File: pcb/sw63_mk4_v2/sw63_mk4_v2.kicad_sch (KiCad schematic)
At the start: 70 parts, among them J1 GT-USB-7070C, J2 SWD, J3 Conn_01x02, Q1 DMG2305UX-7, Q2 DMG2302U-7, Q3 TEMT6200FX01, SW1 KSC321J LFS, SW2 ﻿EVQ-P7J01P, U1 DIO5518BST5, U2 MCP1711T-3.3I/OT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

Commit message: schematic notes
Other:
- note added: "Compatible LED drivers: TLC5916IPWR TLC5917IPWR SCT2167CSSG STP08CP05TTR"
- note added: "R3: 22k = approx 50mA charge current"
- note removed: "22k = approx 50mA charge current"
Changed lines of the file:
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@@
 	(text "BAT current when MCU sleeps (BAT is 4V)\nMCP73832T-2ACI/OT: approx 21uA - little worse\nDIO5518BST5: approx 15uA (10-20 based on ambient temperature) - little better"
 		(exclude_from_sim no)
-		(at 235.712 24.638 0)
+		(at 192.024 26.162 0)
 		(effects
 			(font
@@
 				(thickness 0.1588)
 			)
+			(justify left)
 		)
 	)
@@
 		)
 	)
-	(text "22k = approx 50mA charge current"
+	(text "R3: 22k = approx 50mA charge current"
 		(exclude_from_sim no)
-		(at 237.236 29.464 0)
+		(at 169.164 67.564 0)
 		(effects
 			(font
@@
 				(thickness 0.1588)
 			)
+			(justify left)
 		)
 	)
+	(text "Compatible LED drivers:\nTLC5916IPWR\nTLC5917IPWR\nSCT2167CSSG\nSTP08CP05TTR"
+		(exclude_from_sim no)
+		(at 211.074 133.858 0)
+		(effects
+			(font
+				(size 1.27 1.27)
+				(thickness 0.1588)
+			)
+			(justify left)
+		)
+	)

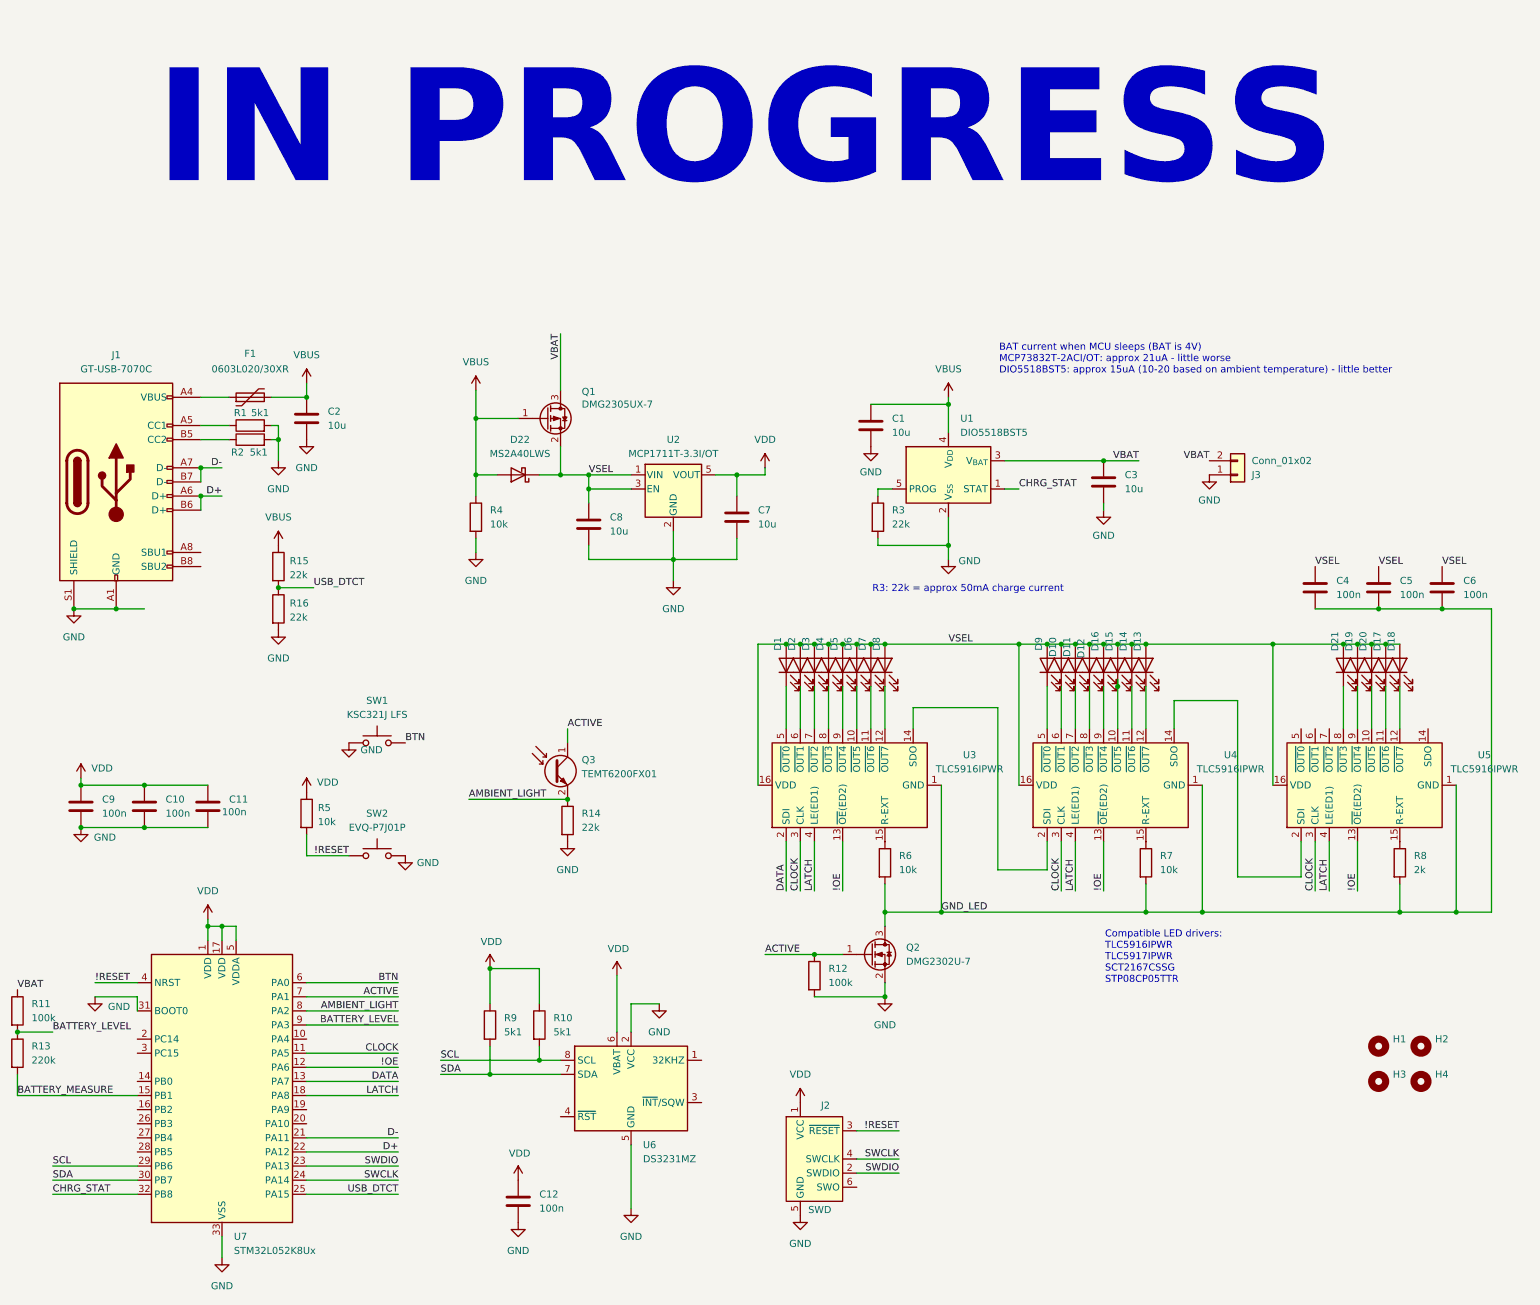
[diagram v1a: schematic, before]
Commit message: update part names and docs
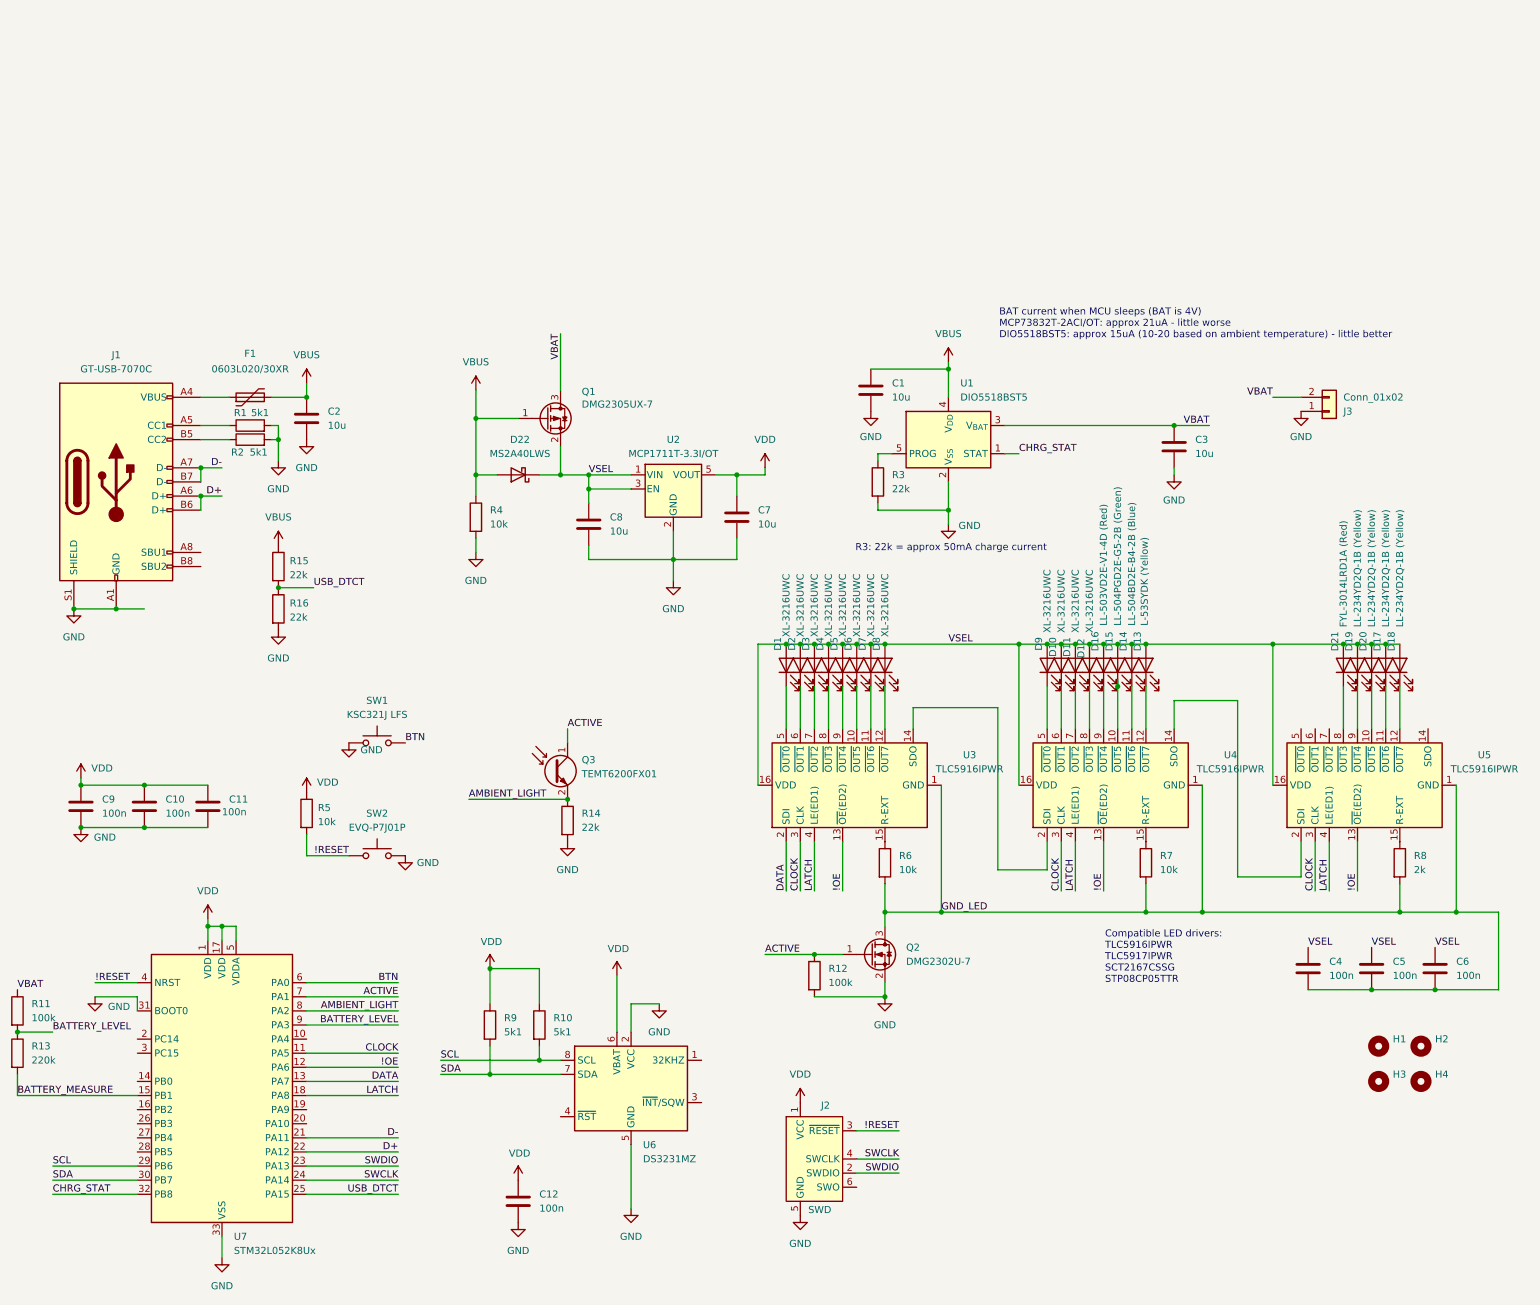
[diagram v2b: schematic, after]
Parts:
- D1, D10, D11, D12, D2, D3, D4, D5, D6, D7, D8, D9: value LED -> XL-3216UWC
- D13: value LED -> L-53SYDK (Yellow)
- D14: value LED -> LL-504BD2E-B4-2B (Blue)
- D15: value LED -> LL-504PGD2E-G5-2B (Green)
- D16: value LED -> LL-503VD2E-V1-4D (Red)
- D17, D18, D19, D20: value LED -> LL-234YD2Q-1B (Yellow)
- D21: value LED -> FYL-3014LRD1A (Red)
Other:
- note removed: "IN PROGRESS"
- moved on the sheet: C1, C3, C4, C5, C6, J3, R3, U1

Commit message: schematic notes and pdf
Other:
- note added: "MCP1711 was chosen because its' low quiescent current"
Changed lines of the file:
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@@
+		)
+	)
+	(text "MCP1711 was chosen because\nits' low quiescent current"
+		(exclude_from_sim no)
+		(at 125.73 28.702 0)
+		(effects
+			(font
+				(size 1.27 1.27)
+				(thickness 0.1588)
+			)
+			(justify left)
 		)
 	)
